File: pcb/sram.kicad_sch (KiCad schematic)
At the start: 0 parts

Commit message: add sram
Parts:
- added U?: IS61WV25616EFBLL, symbol is61wv25616efbll:IS61WV25616EFBLL
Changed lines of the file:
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@@
 (kicad_sch (version 20210406) (generator eeschema)
   (paper "User" 299.999 159.995)
+  (symbol (lib_id "is61wv25616efbll:IS61WV25616EFBLL") (at 144.78 67.31 0) (unit 1)
+    (in_bom yes) (on_board yes) (fields_autoplaced)
+    (property "Reference" "U?" (id 0) (at 144.78 35.56 0))
+    (property "Value" "IS61WV25616EFBLL" (id 1) (at 144.78 38.1 0))
+    (property "Footprint" "" (id 2) (at 144.78 34.29 0)
+      (effects (font (size 1.27 1.27)) hide)
+    )
+    (property "Datasheet" "" (id 3) (at 144.78 34.29 0)
+      (effects (font (size 1.27 1.27)) hide)
+    )
+    (pin "1")
+    (pin "10")
+    (pin "11")
+    (pin "12")
+    (pin "13")
+    (pin "14")
+    (pin "15")
+    (pin "16")
+    (pin "17")
+    (pin "18")
+    (pin "19")
+    (pin "2")
+    (pin "20")
+    (pin "21")
+    (pin "22")
+    (pin "23")
+    (pin "24")
+    (pin "25")
+    (pin "26")
+    (pin "27")
+    (pin "28")
+    (pin "29")
+    (pin "3")
+    (pin "30")
+    (pin "31")
+    (pin "32")
+    (pin "33")
+    (pin "34")
+    (pin "35")
+    (pin "36")
+    (pin "37")
+    (pin "38")
+    (pin "39")
+    (pin "4")
+    (pin "40")
+    (pin "41")
+    (pin "42")
+    (pin "43")
+    (pin "44")
+    (pin "5")
+    (pin "6")
+    (pin "7")
+    (pin "8")
+    (pin "9")
+  )
 )

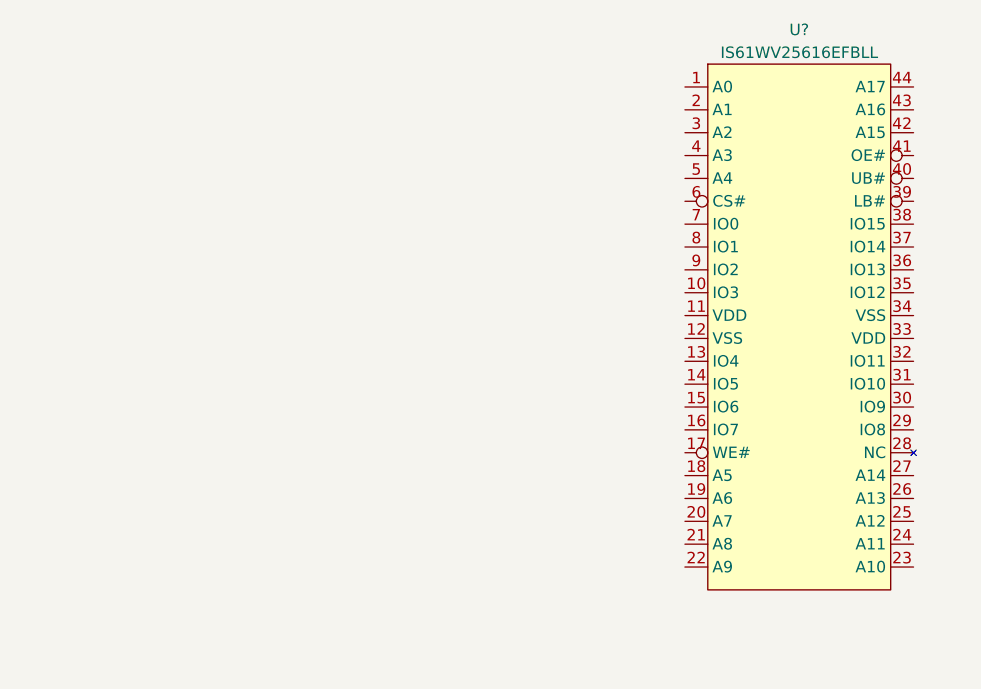
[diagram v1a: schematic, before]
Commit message: route pol
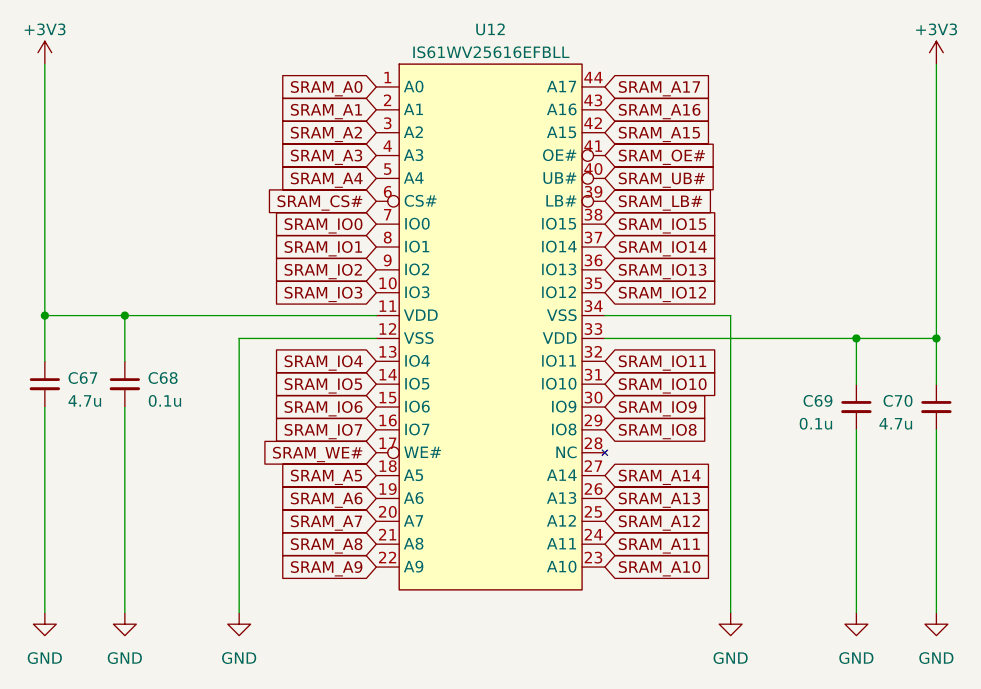
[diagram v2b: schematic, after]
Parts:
- added C67, C70: 4.7u, Capacitor_SMD:CP_Elec_4x4.5, symbol Device:C_Small
- added C68, C69: 0.1u, Capacitor_SMD:C_0402_1005Metric, symbol Device:C_Small
- U12: renamed from U?; footprint (none) -> Package_SO:TSOP-II-44_10.16x18.41mm_P0.8mm
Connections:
- net SRAM_A0: now reaches U12.1 (A0)
- net SRAM_IO3: now reaches U12.10 (IO3)
- net +3V3: now reaches U12.11 (VDD)
- net +3V3: now also U12.33 (VDD), C67.1, C68.1, C69.1, C70.1
- net GND: now reaches U12.12 (VSS)
- net GND: now also U12.34 (VSS), C67.2, C68.2, C69.2, C70.2
- net SRAM_IO4: now reaches U12.13 (IO4)
- net SRAM_IO5: now reaches U12.14 (IO5)
- net SRAM_IO6: now reaches U12.15 (IO6)
- net SRAM_IO7: now reaches U12.16 (IO7)
- net SRAM_WE#: now reaches U12.17 (WE#)
- net SRAM_A5: now reaches U12.18 (A5)
- net SRAM_A6: now reaches U12.19 (A6)
- net SRAM_A1: now reaches U12.2 (A1)
- net SRAM_A7: now reaches U12.20 (A7)
- net SRAM_A8: now reaches U12.21 (A8)
- net SRAM_A9: now reaches U12.22 (A9)
- net SRAM_A10: now reaches U12.23 (A10)
- net SRAM_A11: now reaches U12.24 (A11)
- net SRAM_A12: now reaches U12.25 (A12)
- net SRAM_A13: now reaches U12.26 (A13)
- net SRAM_A14: now reaches U12.27 (A14)
- net SRAM_IO8: now reaches U12.29 (IO8)
- net SRAM_A2: now reaches U12.3 (A2)
- net SRAM_IO9: now reaches U12.30 (IO9)
- net SRAM_IO10: now reaches U12.31 (IO10)
- net SRAM_IO11: now reaches U12.32 (IO11)
- net SRAM_IO12: now reaches U12.35 (IO12)
- net SRAM_IO13: now reaches U12.36 (IO13)
- net SRAM_IO14: now reaches U12.37 (IO14)
- net SRAM_IO15: now reaches U12.38 (IO15)
- net SRAM_LB#: now reaches U12.39 (LB#)
- net SRAM_A3: now reaches U12.4 (A3)
- net SRAM_UB#: now reaches U12.40 (UB#)
- net SRAM_OE#: now reaches U12.41 (OE#)
- net SRAM_A15: now reaches U12.42 (A15)
- net SRAM_A16: now reaches U12.43 (A16)
- net SRAM_A17: now reaches U12.44 (A17)
- net SRAM_A4: now reaches U12.5 (A4)
- net SRAM_CS#: now reaches U12.6 (CS#)
- net SRAM_IO0: now reaches U12.7 (IO0)
- net SRAM_IO1: now reaches U12.8 (IO1)
- net SRAM_IO2: now reaches U12.9 (IO2)
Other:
- moved on the sheet: U12

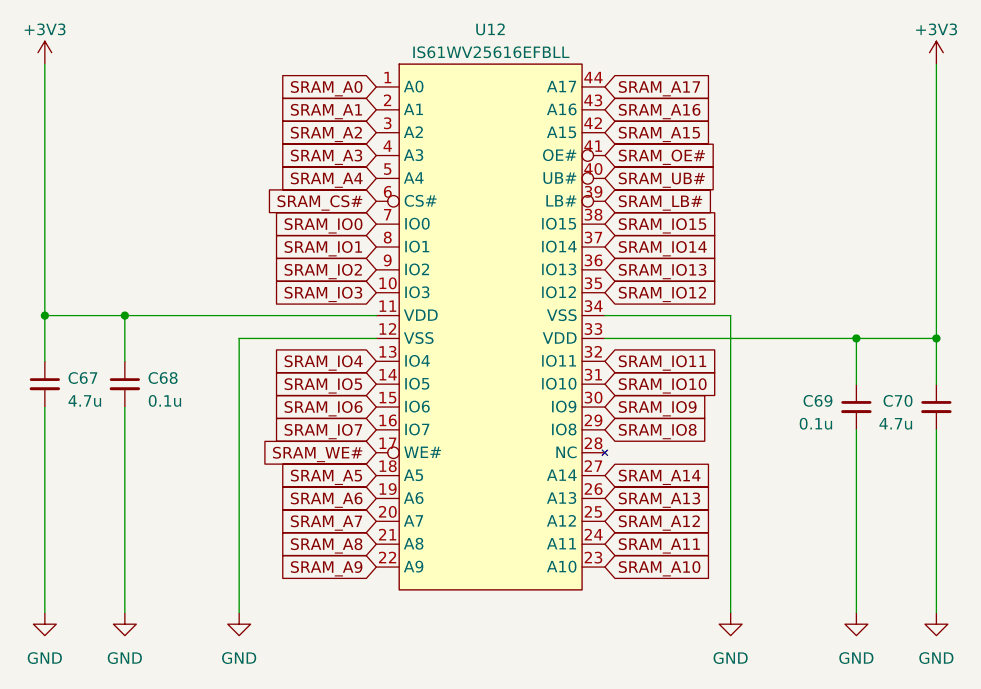
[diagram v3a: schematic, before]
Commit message: added silkscreen values
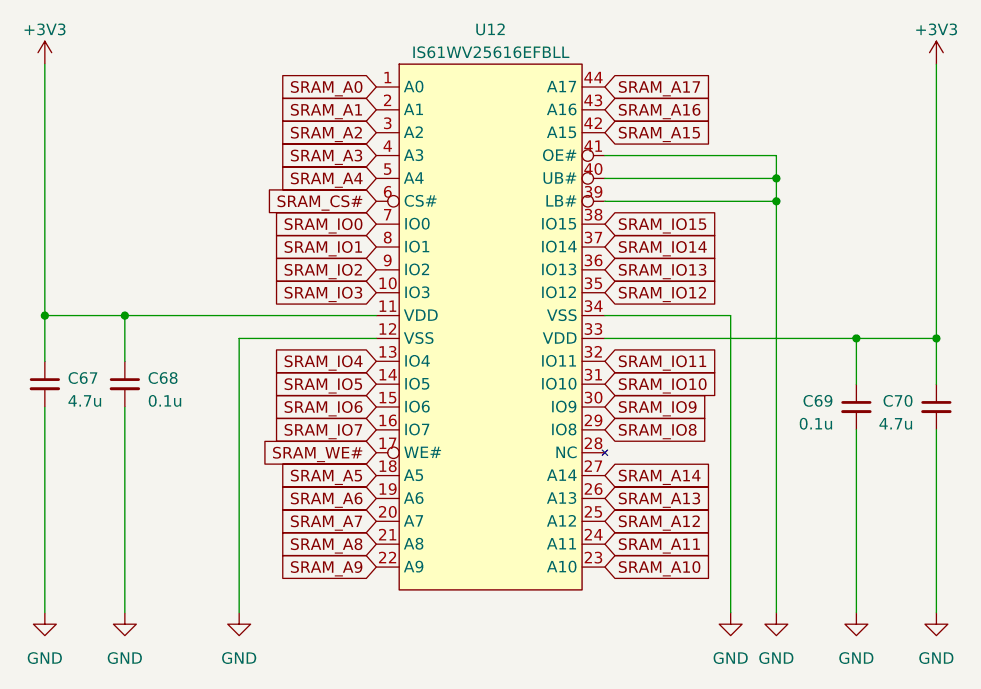
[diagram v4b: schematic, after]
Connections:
- net SRAM_LB# is gone; now on net GND: U12.39 (LB#)
- net SRAM_OE# is gone; now on net GND: U12.41 (OE#)
- net SRAM_UB# is gone; now on net GND: U12.40 (UB#)
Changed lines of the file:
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@@
   (junction (at 60.96 67.31) (diameter 0.9144) (color 0 0 0 0))
   (junction (at 69.85 67.31) (diameter 0.9144) (color 0 0 0 0))
+  (junction (at 142.24 52.07) (diameter 0.9144) (color 0 0 0 0))
+  (junction (at 142.24 54.61) (diameter 0.9144) (color 0 0 0 0))
   (junction (at 151.13 69.85) (diameter 0.9144) (color 0 0 0 0))
   (junction (at 160.02 69.85) (diameter 0.9144) (color 0 0 0 0))
@@
     (stroke (width 0) (type solid) (color 0 0 0 0))
   )
+  (wire (pts (xy 123.19 49.53) (xy 142.24 49.53))
+    (stroke (width 0) (type solid) (color 0 0 0 0))
+  )
+  (wire (pts (xy 123.19 54.61) (xy 142.24 54.61))
+    (stroke (width 0) (type solid) (color 0 0 0 0))
+  )
   (wire (pts (xy 123.19 67.31) (xy 137.16 67.31))
     (stroke (width 0) (type solid) (color 0 0 0 0))
@@
     (stroke (width 0) (type solid) (color 0 0 0 0))
   )
+  (wire (pts (xy 142.24 49.53) (xy 142.24 52.07))
+    (stroke (width 0) (type solid) (color 0 0 0 0))
+  )
+  (wire (pts (xy 142.24 52.07) (xy 123.19 52.07))
+    (stroke (width 0) (type solid) (color 0 0 0 0))
+  )
+  (wire (pts (xy 142.24 54.61) (xy 142.24 52.07))
+    (stroke (width 0) (type solid) (color 0 0 0 0))
+  )
+  (wire (pts (xy 142.24 100.33) (xy 142.24 54.61))
+    (stroke (width 0) (type solid) (color 0 0 0 0))
+  )
   (wire (pts (xy 151.13 69.85) (xy 151.13 74.93))
     (stroke (width 0) (type solid) (color 0 0 0 0))
@@
     (effects (font (size 1.27 1.27)) (justify left))
     (property "Intersheet References" "${INTERSHEET_REFS}" (id 0) (at 135.0979 46.9106 0)
-      (effects (font (size 1.27 1.27)) (justify left) hide)
-    )
-  )
-  (global_label "SRAM_OE#" (shape input) (at 123.19 49.53 0) (fields_autoplaced)
-    (effects (font (size 1.27 1.27)) (justify left))
-    (property "Intersheet References" "${INTERSHEET_REFS}" (id 0) (at 135.3398 49.4506 0)
-      (effects (font (size 1.27 1.27)) (justify left) hide)
-    )
-  )
-  (global_label "SRAM_UB#" (shape input) (at 123.19 52.07 0) (fields_autoplaced)
-    (effects (font (size 1.27 1.27)) (justify left))
-    (property "Intersheet References" "${INTERSHEET_REFS}" (id 0) (at 135.4607 51.9906 0)
-      (effects (font (size 1.27 1.27)) (justify left) hide)
-    )
-  )
-  (global_label "SRAM_LB#" (shape input) (at 123.19 54.61 0) (fields_autoplaced)
-    (effects (font (size 1.27 1.27)) (justify left))
-    (property "Intersheet References" "${INTERSHEET_REFS}" (id 0) (at 135.1583 54.5306 0)
       (effects (font (size 1.27 1.27)) (justify left) hide)
     )
@@
       (effects (font (size 1.27 1.27)) hide)
     )
+    (pin "1")
+  )
+  (symbol (lib_id "power:GND") (at 142.24 100.33 0) (unit 1)
+    (in_bom yes) (on_board yes) (fields_autoplaced)
+    (property "Reference" "#PWR0137" (id 0) (at 142.24 106.68 0)
+      (effects (font (size 1.27 1.27)) hide)
+    )
+    (property "Value" "GND" (id 1) (at 142.24 105.41 0))
+    (property "Footprint" "" (id 2) (at 142.24 100.33 0)
+      (effects (font (size 1.27 1.27)) hide)
+    )
+    (property "Datasheet" "" (id 3) (at 142.24 100.33 0)
+      (effects (font (size 1.27 1.27)) hide)
+    )
